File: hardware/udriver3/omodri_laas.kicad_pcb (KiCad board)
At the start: 2 copper layers, 326 parts, among them J1 Conn_01x12, J10 Conn_02x04_Odd_Even, J11 Conn_01x08, J12 Conn_01x08, J2 Conn_01x05, J3 Conn_01x04, J4 Conn_01x02, J5 Conn_01x03, J6 Conn_01x03, J7 Conn_01x05, J8 Conn_01x05, J9 Conn_01x02, Q1 BSC028N06LS3, Q10 BSC028N06LS3, Q11 BSC028N06LS3, Q12 BSC028N06LS3, Q13 BSC028N06LS3, Q14 BSC028N06LS3, Q15 BSC028N06LS3, Q16 CSD88599Q5DC, Q17 CSD88599Q5DC, Q18 CSD88599Q5DC, Q2 BSC028N06LS3, Q3 BSC028N06LS3, Q4 BSC028N06LS3, Q5 BSC028N06LS3, Q6 BSC028N06LS3, Q7 CSD88599Q5DC, Q8 CSD88599Q5DC, Q9 CSD88599Q5DC, SW1 B3U-3100P, U1 DRV8353S, U10 TCAN332G, U11 TPS3703, U12 TPS3703, U13 TPD6E05U06, U14 DSLVDS1048, U15 TPD6E05U06, U16 DSLVDS1047, U17 TPD2E001, U18 TPD2E001, U19 TPD2E001, U2 DRV8353S, U20 TPD2E001, U3 LMZ36002, U4 TMS320F28388D, U5 MPM3804GG, U6 MPM3804GG, U7 REF6230, U8 OPA388, U9 TXB0106, X1 ECS-TXO-2016-33-200-TR

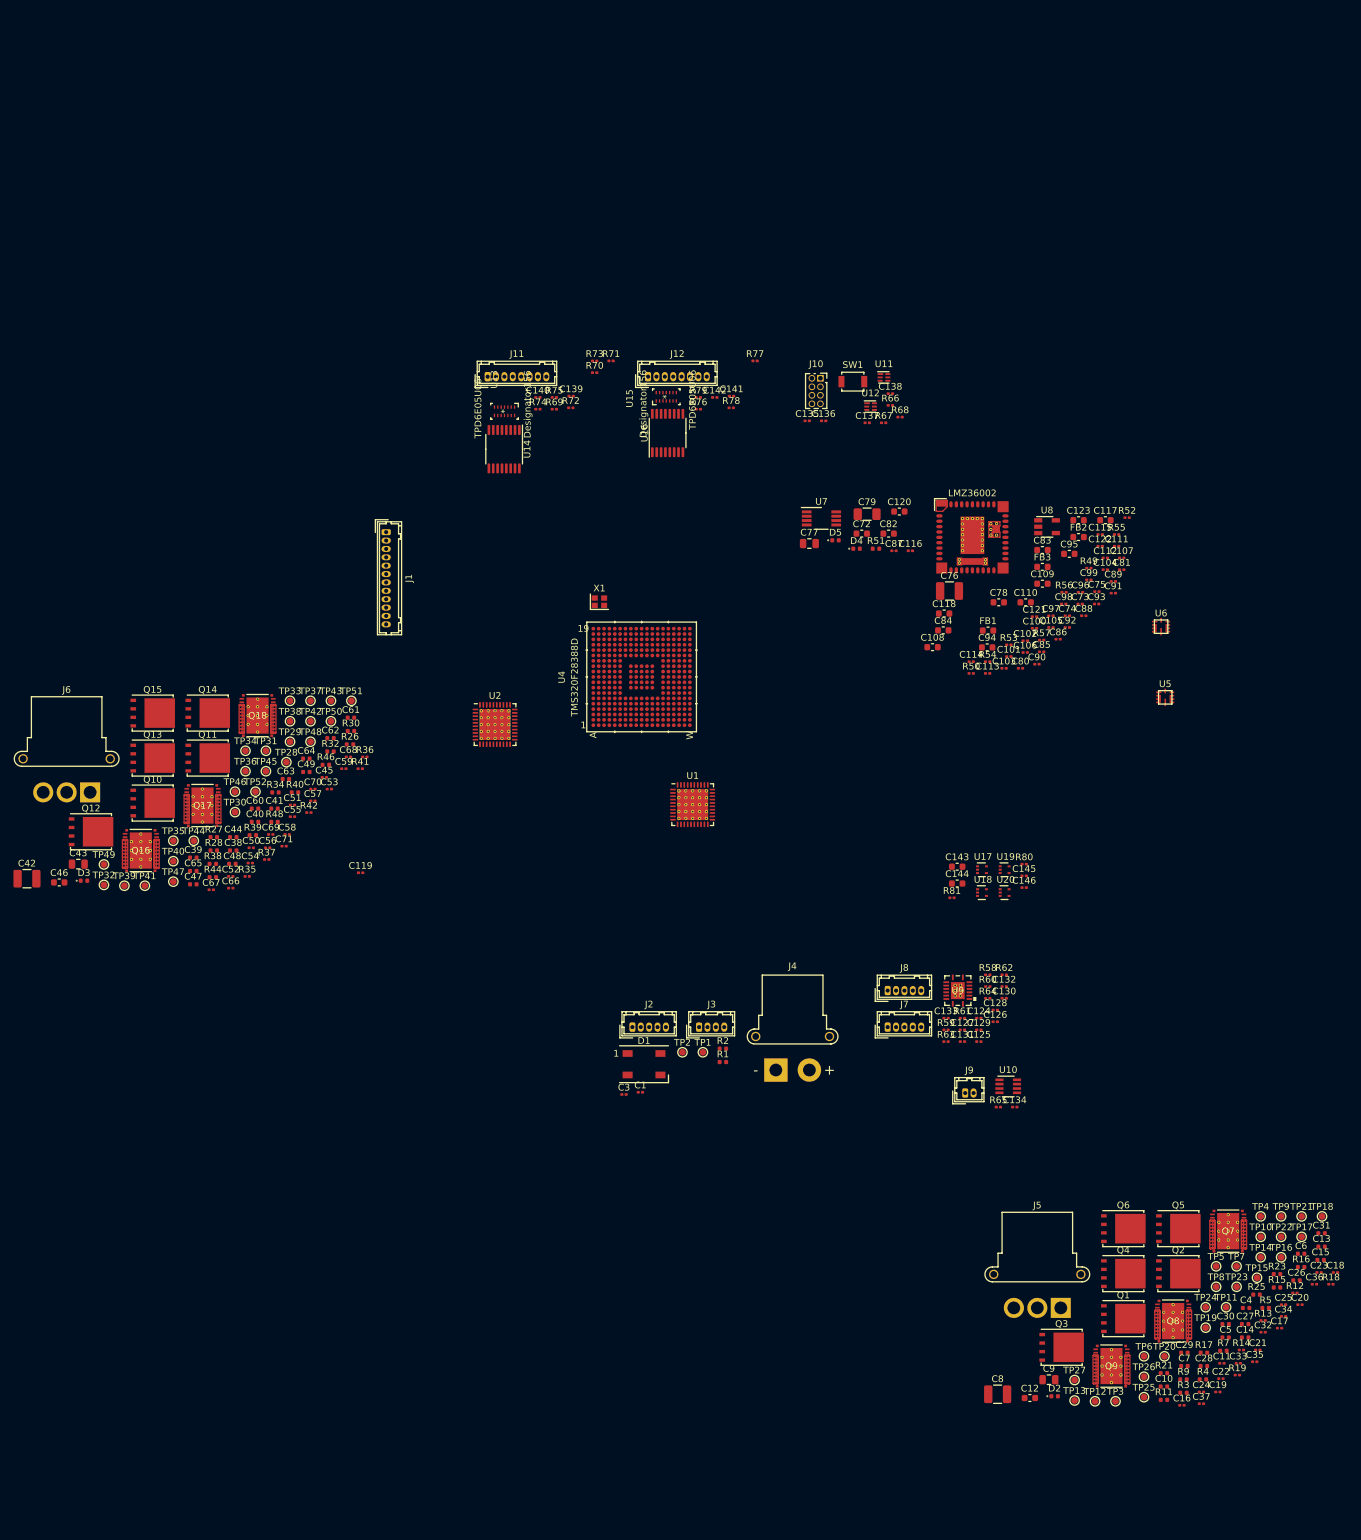
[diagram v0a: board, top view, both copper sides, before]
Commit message: First complete release. No EtherCAT, IO ready to be connected.
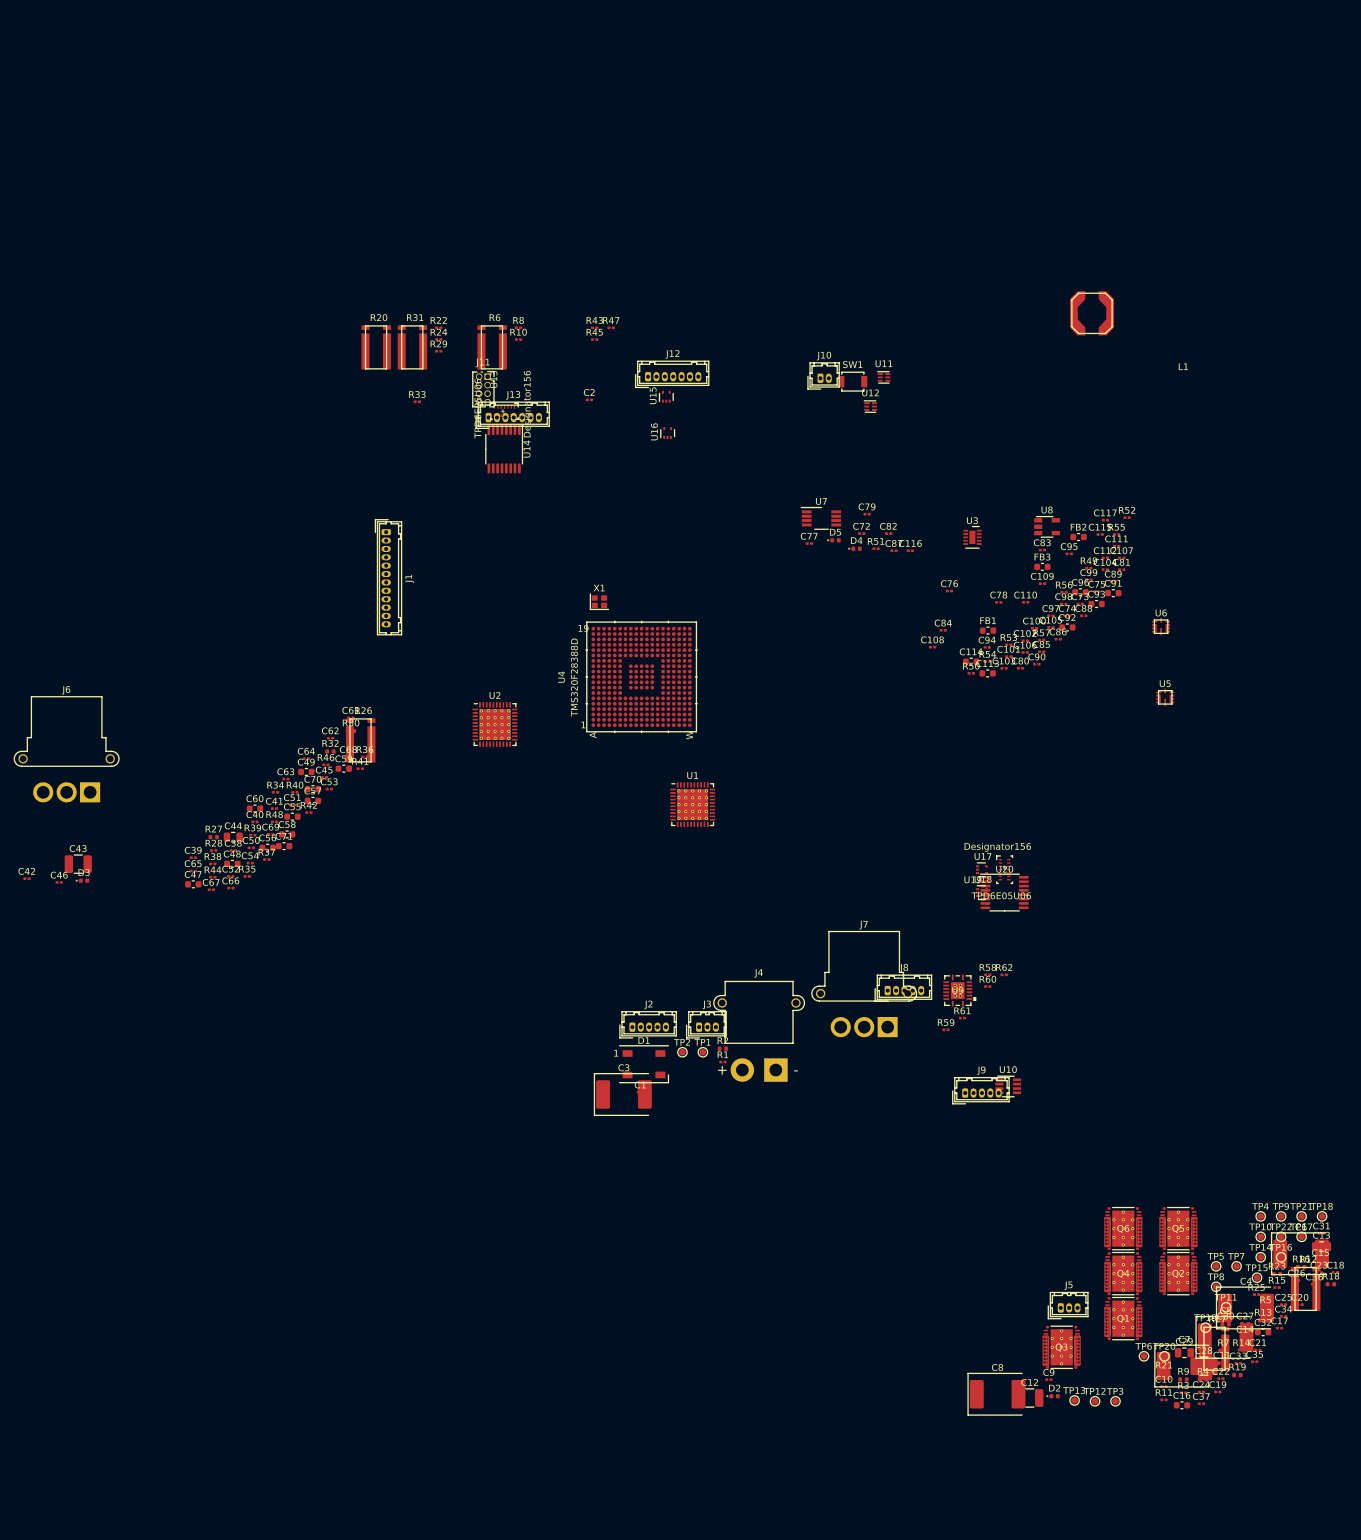
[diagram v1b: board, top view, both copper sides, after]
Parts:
- removed C118, C120, C123, C143, C144: 10uF, Capacitor_SMD:C_0603_1608Metric
- removed C119, C121, C128, C129, C134, C135, C136, C138, C140, C142, C145, C146: 100nF, Capacitor_SMD:C_0201_0603Metric
- removed C122, C127, C133, C139, C141: 1uF, Capacitor_SMD:C_0201_0603Metric
- removed C124, C125, C126, C130, C131, C132: 1nF, Capacitor_SMD:C_0201_0603Metric
- removed C137: 10nF, Capacitor_SMD:C_0201_0603Metric
- removed Q10, Q11, Q12, Q13, Q14, Q15: BSC028N06LS3, Package_TO_SOT_SMD:TDSON-8-1
- removed Q16, Q17, Q18, Q7, Q8, Q9: CSD88599Q5DC, udrive3:VSON_CLIP_22
- removed R63, R64, R68: 1k, Resistor_SMD:R_0201_0603Metric
- removed R65: 120, Resistor_SMD:R_0201_0603Metric
- removed R66, R67, R72, R73, R74, R75, R76, R77, R78, R79: 10k, Resistor_SMD:R_0201_0603Metric
- removed R69, R70, R71: 100, Resistor_SMD:R_0201_0603Metric
- removed R80, R81: 0.1, Resistor_SMD:R_0201_0603Metric
- removed TP23, TP24, TP25, TP26, TP27, TP28, TP29, TP30, TP31, TP32, TP33, TP34, TP35, TP36, TP37, TP38, TP39, TP40, TP41, TP42, TP43, TP44, TP45, TP46, TP47, TP48, TP49, TP50, TP51, TP52: TestPoint, TestPoint:TestPoint_Pad_D1.0mm
- added C2: 10nF, Capacitor_SMD:C_0201_0603Metric, F.Cu at (110.3, -18.5)
- added J13: Conn_01x07, Connector_Hirose:Hirose_DF13-07P-1.25DSA_1x07_P1.25mm_Vertical, F.Cu at (95.3, -15.8)
- added L1: 22uH, udrive3:L_coilcraft_LPS62xx, F.Cu at (185.3, -31.4)
- added R10: 120, Resistor_SMD:R_0201_0603Metric, F.Cu at (99.7, -27.5)
- added R20: 0.005, udrive3:FC4L64, F.Cu at (76.9, -25.7)
- added R22: 120, Resistor_SMD:R_0201_0603Metric, F.Cu at (87.9, -29.2)
- added R24: 120, Resistor_SMD:R_0201_0603Metric, F.Cu at (87.9, -27.5)
- added R29: 10k, Resistor_SMD:R_0201_0603Metric, F.Cu at (87.9, -25.7)
- added R31: 0.005, udrive3:FC4L64, F.Cu at (82.3, -25.7)
- added R33: 10k, Resistor_SMD:R_0201_0603Metric, F.Cu at (84.7, -18.2)
- added R43: 1k, Resistor_SMD:R_0201_0603Metric, F.Cu at (111.1, -29.2)
- added R45: 1k, Resistor_SMD:R_0201_0603Metric, F.Cu at (111.1, -27.5)
- added R47: 1k, Resistor_SMD:R_0201_0603Metric, F.Cu at (113.6, -29.2)
- added R6: 0.005, udrive3:FC4L64, F.Cu at (94.2, -25.7)
- added R8: 120, Resistor_SMD:R_0201_0603Metric, F.Cu at (99.7, -29.2)
- C10, C38: value 1uF -> 10nF; footprint Capacitor_SMD:C_0402_1005Metric -> Capacitor_SMD:C_0201_0603Metric
- C100, C106, C87, C88, C89, C90: value 100nF -> 1uF
- C103, C104, C105, C97, C98, C99: value 100nF -> 1nF
- C108, C109, C117, C72, C82, C83, C84, C94: value 10uF -> 100nF; footprint Capacitor_SMD:C_0603_1608Metric -> Capacitor_SMD:C_0201_0603Metric
- C11: footprint Capacitor_SMD:C_0201_0603Metric -> Capacitor_SMD:C_0402_1005Metric
- C110: value 10uF -> 10nF; footprint Capacitor_SMD:C_0603_1608Metric -> Capacitor_SMD:C_0201_0603Metric
- C113, C114, C91, C92, C93: value 1uF -> 10uF; footprint Capacitor_SMD:C_0201_0603Metric -> Capacitor_SMD:C_0603_1608Metric
- C115, C116, C74, C80: value 1uF -> 100nF
- C12: value 47nF -> 10uF; footprint Capacitor_SMD:C_0603_1608Metric -> Capacitor_SMD:C_1210_3225Metric
- C13, C29: value 1nF -> 100nF; footprint Capacitor_SMD:C_0402_1005Metric -> Capacitor_SMD:C_0805_2012Metric
- C14, C27, C30, C51, C67, C68: value 1nF -> 1uF
- C15, C31: value 1nF -> 1uF; footprint Capacitor_SMD:C_0402_1005Metric -> Capacitor_SMD:C_0201_0603Metric
- C16, C32: value 1nF -> 47nF; footprint Capacitor_SMD:C_0201_0603Metric -> Capacitor_SMD:C_0603_1608Metric
- C18, C34: value 1nF -> 10nF
- C19, C35, C54: value 10nF -> 100nF
- C22: value 100nF -> 10nF
- C23, C25: value 10nF -> 1nF
- C26, C40: value 1nF -> 10nF; footprint Capacitor_SMD:C_0402_1005Metric -> Capacitor_SMD:C_0201_0603Metric
- C28: value 1nF -> 10uF; footprint Capacitor_SMD:C_0402_1005Metric -> Capacitor_SMD:C_1210_3225Metric
- C3: value 10nF -> 100uF; footprint Capacitor_SMD:C_0201_0603Metric -> Capacitor_Tantalum_SMD:CP_EIA-7360-38_Kemet-E
- C39, C41: footprint Capacitor_SMD:C_0402_1005Metric -> Capacitor_SMD:C_0201_0603Metric
- C4: value 1uF -> 100uF; footprint Capacitor_SMD:C_0402_1005Metric -> Capacitor_Tantalum_SMD:CP_EIA-7360-38_Kemet-E
- C42: value 10uF -> 10nF; footprint Capacitor_SMD:C_1210_3225Metric -> Capacitor_SMD:C_0201_0603Metric
- C43: value 100nF -> 10uF; footprint Capacitor_SMD:C_0805_2012Metric -> Capacitor_SMD:C_1210_3225Metric
- C44: value 1uF -> 100nF; footprint Capacitor_SMD:C_0402_1005Metric -> Capacitor_SMD:C_0805_2012Metric
- C45: value 1uF -> 10nF
- C46: value 47nF -> 1uF; footprint Capacitor_SMD:C_0603_1608Metric -> Capacitor_SMD:C_0201_0603Metric
- C47, C48, C49, C60: value 1nF -> 10uF; footprint Capacitor_SMD:C_0402_1005Metric -> Capacitor_SMD:C_0603_1608Metric
- C5, C6, C7: value 1nF -> 100uF; footprint Capacitor_SMD:C_0402_1005Metric -> Capacitor_Tantalum_SMD:CP_EIA-7360-38_Kemet-E
- C50, C52, C66: value 1nF -> 100nF
- C53, C69: value 10nF -> 1uF
- C55, C57, C58, C59, C70, C71: value 10nF -> 10uF; footprint Capacitor_SMD:C_0201_0603Metric -> Capacitor_SMD:C_0603_1608Metric
- C56, C96: value 100nF -> 10uF; footprint Capacitor_SMD:C_0201_0603Metric -> Capacitor_SMD:C_0603_1608Metric
- C61, C62, C63, C64, C65: value 1nF -> 100nF; footprint Capacitor_SMD:C_0402_1005Metric -> Capacitor_SMD:C_0201_0603Metric
- C76: value 10uF -> 100nF; footprint Capacitor_SMD:C_1210_3225Metric -> Capacitor_SMD:C_0201_0603Metric
- C77: footprint Capacitor_SMD:C_0805_2012Metric -> Capacitor_SMD:C_0201_0603Metric
- C78: value 47nF -> 100nF; footprint Capacitor_SMD:C_0603_1608Metric -> Capacitor_SMD:C_0201_0603Metric
- C79: value 100uF -> 100nF; footprint Capacitor_SMD:C_1206_3216Metric -> Capacitor_SMD:C_0201_0603Metric
- C8: value 10uF -> 100uF; footprint Capacitor_SMD:C_1210_3225Metric -> Capacitor_Tantalum_SMD:CP_EIA-7360-38_Kemet-E
- C9: value 100nF -> 10nF; footprint Capacitor_SMD:C_0805_2012Metric -> Capacitor_SMD:C_0201_0603Metric
- C95: value 10uF -> 1uF; footprint Capacitor_SMD:C_0603_1608Metric -> Capacitor_SMD:C_0201_0603Metric
- J10: value Conn_02x04_Odd_Even -> Conn_01x02; footprint Connector_PinSocket_1.27mm:PinSocket_2x04_P1.27mm_Vertical -> Connector_Hirose:Hirose_DF13-02P-1.25DSA_1x02_P1.25mm_Vertical
- J11: value Conn_01x08 -> Conn_02x04_Odd_Even; footprint Connector_Hirose:Hirose_DF13-08P-1.25DSA_1x08_P1.25mm_Vertical -> Connector_PinSocket_1.27mm:PinSocket_2x04_P1.27mm_Vertical
- J12: value Conn_01x08 -> Conn_01x07; footprint Connector_Hirose:Hirose_DF13-08P-1.25DSA_1x08_P1.25mm_Vertical -> Connector_Hirose:Hirose_DF13-07P-1.25DSA_1x07_P1.25mm_Vertical
- J3: value Conn_01x04 -> Conn_01x03; footprint Connector_Hirose:Hirose_DF13-04P-1.25DSA_1x04_P1.25mm_Vertical -> Connector_Hirose:Hirose_DF13-03P-1.25DSA_1x03_P1.25mm_Vertical
- J4: footprint Connector_AMASS:AMASS_XT30PW-F_1x02_P2.50mm_Horizontal -> Connector_AMASS:AMASS_XT30PW-M_1x02_P2.50mm_Horizontal
- J5: footprint Connector_AMASS:AMASS_MR30PW-FB_1x03_P3.50mm_Horizontal -> Connector_Hirose:Hirose_DF13-03P-1.25DSA_1x03_P1.25mm_Vertical
- J7: value Conn_01x05 -> Conn_01x03; footprint Connector_Hirose:Hirose_DF13-05P-1.25DSA_1x05_P1.25mm_Vertical -> Connector_AMASS:AMASS_MR30PW-FB_1x03_P3.50mm_Horizontal
- J9: value Conn_01x02 -> Conn_01x05; footprint Connector_Hirose:Hirose_DF13-02P-1.25DSA_1x02_P1.25mm_Vertical -> Connector_Hirose:Hirose_DF13-05P-1.25DSA_1x05_P1.25mm_Vertical
- Q1, Q2, Q3, Q4, Q5, Q6: value BSC028N06LS3 -> CSD88599Q5DC; footprint Package_TO_SOT_SMD:TDSON-8-1 -> udrive3:VSON_CLIP_22
- R1, R3: value 100k -> 120; footprint Resistor_SMD:R_0402_1005Metric -> Resistor_SMD:R_0201_0603Metric
- R11, R25, R48: value 5.1k -> 120; footprint Resistor_SMD:R_0402_1005Metric -> Resistor_SMD:R_0201_0603Metric
- R12: value 100 -> 0.005; footprint Resistor_SMD:R_0201_0603Metric -> udrive3:FC4L64
- R13: value 100 -> 5.1k; footprint Resistor_SMD:R_0201_0603Metric -> Resistor_SMD:R_0402_1005Metric
- R14, R37: value 100 -> 220
- R15: value 100k -> 10k; footprint Resistor_SMD:R_0402_1005Metric -> Resistor_SMD:R_0201_0603Metric
- R17, R26: value 100k -> 0.005; footprint Resistor_SMD:R_0402_1005Metric -> udrive3:FC4L64
- R18: value 220 -> 5.1k; footprint Resistor_SMD:R_0201_0603Metric -> Resistor_SMD:R_0402_1005Metric
- R19: value 10k -> 100k; footprint Resistor_SMD:R_0201_0603Metric -> Resistor_SMD:R_0402_1005Metric
- R2, R23, R30, R9: value 5.1k -> 100k
- R27, R4: value 100k -> 5.1k
- R28: value 100k -> 220; footprint Resistor_SMD:R_0402_1005Metric -> Resistor_SMD:R_0201_0603Metric
- R34: value 5.1k -> 470; footprint Resistor_SMD:R_0402_1005Metric -> Resistor_SMD:R_0201_0603Metric
- R35: value 100 -> 100k
- R36: value 100 -> 22.1k
- R38, R39: footprint Resistor_SMD:R_0402_1005Metric -> Resistor_SMD:R_0201_0603Metric
- R40: value 100k -> 56; footprint Resistor_SMD:R_0402_1005Metric -> Resistor_SMD:R_0201_0603Metric
- R41: value 220 -> 1k
- R42: value 10k -> 1k
- R44, R46, R51: value 5.1k -> 1k; footprint Resistor_SMD:R_0402_1005Metric -> Resistor_SMD:R_0201_0603Metric
- R49: value 470 -> 10k
- R50: value 150k -> 10k
- R52: value 100k -> 100
- R53: value 22.1k -> 100
- R54: value 220 -> 100
- R55: value 56 -> 10k
- R56, R57: value 100k -> 10k
- R58, R59: value 1k -> 0.1
- R60, R61, R62: value 1k -> 10k
- U15: value TPD6E05U06 -> TPD2E001; footprint udrive3:USON_14 -> Package_SO:Texas_R-PDSO-N5
- U16: value DSLVDS1047 -> TPD2E001; footprint Package_SO:TSSOP-16_4.4x5mm_P0.65mm -> Package_SO:Texas_R-PDSO-N5
- U19: value TPD2E001 -> TPD6E05U06; footprint Package_SO:Texas_R-PDSO-N5 -> udrive3:USON_14
- U20: value TPD2E001 -> DSLVDS1047; footprint Package_SO:Texas_R-PDSO-N5 -> Package_SO:TSSOP-16_4.4x5mm_P0.65mm
- U3: value LMZ36002 -> MAX17502FxTB; footprint udrive3:B3QFN_43 -> Package_DFN_QFN:TDFN-10-1EP_2x3mm_P0.5mm_EP0.9x2mm
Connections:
- C10 pad 1: GND -> /F2838x GPIOs/ANALOG_IN1
- C10 pad 2: /DRV driver for motor2/VGLS -> GND
- C100 pad 1: VDD_3V3 -> 5V0
- C102 pad 1: VDD_3V3 -> 5V0
- C103 pad 1: VDD_3V3 -> /Quadrature Encoders for motor 1 & 2/ENC2_A
- C104 pad 1: VDD_3V3 -> /Quadrature Encoders for motor 1 & 2/ENC2_B
- C105 pad 1: VDD_3V3 -> /Quadrature Encoders for motor 1 & 2/ENC2_I
- C106 pad 1: VDD_3V3 -> 5V0
- C108 pad 1: 5V0 -> VDD_3V3
- C109 pad 1: /Power distribution/1V2 -> VDD_3V3
- C11 pad 1: /DRV driver for motor2/DVDD -> VPOWER
- C11 pad 2: GND -> Net-(C11-Pad2)
- C110 pad 1: /Power distribution/1V2 -> /JTAG Bus + Oscillator + Reset/~XRSn~
- C113 pad 1: VDD_3V3 -> Net-(C113-Pad1)
- C114 pad 1: VDD_3V3 -> Net-(C114-Pad1)
- C115 pad 1: VDD_3V3 -> REF_3V0_BUF
- C116 pad 1: VDD_3V3 -> REF_3V0_BUF
- C12 pad 1: Net-(C12-Pad1) -> VPOWER
- C12 pad 2: Net-(C12-Pad2) -> GND
- C13 pad 1: /DRV driver for motor2/GLA -> VPOWER
- C13 pad 2: Net-(C13-Pad2) -> GND
- C14 pad 1: /DRV driver for motor2/GLB -> GND
- C14 pad 2: Net-(C14-Pad2) -> /DRV driver for motor2/VGLS
- C15 pad 1: /DRV driver for motor2/GLC -> /DRV driver for motor2/DVDD
- C15 pad 2: Net-(C15-Pad2) -> GND
- C16 pad 1: /DRV driver for motor2/SPA -> Net-(C16-Pad1)
- C16 pad 2: /DRV driver for motor2/SNA -> Net-(C16-Pad2)
- C17 pad 1: /DRV driver for motor2/SPB -> /DRV driver for motor2/SPA
- C17 pad 2: /DRV driver for motor2/SNB -> /DRV driver for motor2/SNA
- C18 pad 1: /DRV driver for motor2/SPC -> /F2838x GPIOs/M2_Va
- C18 pad 2: /DRV driver for motor2/SNC -> GND
- C19 pad 1: /F2838x GPIOs/M2_Va -> REF_3V0_BUF
- C20 pad 1: /F2838x GPIOs/M2_Vb -> /F2838x GPIOs/M2_Ic
- C21 pad 1: /F2838x GPIOs/M2_Vc -> /F2838x GPIOs/M2_Ib
- C22 pad 1: REF_3V0_BUF -> /F2838x GPIOs/M2_Ia
- C23 pad 1: /F2838x GPIOs/M2_Ic -> /DRV driver for motor2/SPB
- C23 pad 2: GND -> /DRV driver for motor2/SNB
- C24 pad 1: /F2838x GPIOs/M2_Ib -> /F2838x GPIOs/M2_Vb
- C25 pad 1: /F2838x GPIOs/M2_Ia -> /DRV driver for motor2/SPC
- C25 pad 2: GND -> /DRV driver for motor2/SNC
- C26 pad 1: /DRV driver for motor2/GHA -> /F2838x GPIOs/M2_Vc
- C26 pad 2: /DRV driver for motor2/MOTOR_CH1 -> GND
- C27 pad 1: /DRV driver for motor2/GHB -> VPOWER
- C27 pad 2: /DRV driver for motor2/MOTOR_CH2 -> Net-(C27-Pad2)
- C28 pad 1: /DRV driver for motor2/GHC -> VPOWER
- C28 pad 2: /DRV driver for motor2/MOTOR_CH3 -> GND
- C29 pad 1: /DRV driver for motor2/GLA -> VPOWER
- C29 pad 2: PGND -> GND
- C3 pad 1: /F2838x GPIOs/M1_Vbus -> VPOWER
- C3 pad 2: GND -> Net-(C3-Pad2)
- C30 pad 1: /DRV driver for motor2/GLB -> GND
- C30 pad 2: PGND -> /DRV driver for motor1/VGLS
- C31 pad 1: /DRV driver for motor2/GLC -> /DRV driver for motor1/DVDD
- C31 pad 2: PGND -> GND
- C32 pad 1: /DRV driver for motor2/SPA -> Net-(C32-Pad1)
- C32 pad 2: /DRV driver for motor2/SNA -> Net-(C32-Pad2)
- C33 pad 1: /DRV driver for motor2/SPB -> /DRV driver for motor1/SPA
- C33 pad 2: /DRV driver for motor2/SNB -> /DRV driver for motor1/SNA
- C34 pad 1: /DRV driver for motor2/SPC -> /F2838x GPIOs/M1_Va
- C34 pad 2: /DRV driver for motor2/SNC -> GND
- C35 pad 1: /F2838x GPIOs/M2_Va -> REF_3V0_BUF
- C36 pad 1: /F2838x GPIOs/M2_Vb -> /F2838x GPIOs/M1_Ic
- C37 pad 1: /F2838x GPIOs/M2_Vc -> /F2838x GPIOs/M1_Ib
- C38 pad 1: VPOWER -> /F2838x GPIOs/M1_Ia
- C38 pad 2: Net-(C38-Pad2) -> GND
- C39 pad 1: /DRV driver for motor1/GHA -> /DRV driver for motor1/SPB
- C39 pad 2: /DRV driver for motor1/MOTOR_CH1 -> /DRV driver for motor1/SNB
- C40 pad 1: /DRV driver for motor1/GHB -> /F2838x GPIOs/M1_Vb
- C40 pad 2: /DRV driver for motor1/MOTOR_CH2 -> GND
- C41 pad 1: /DRV driver for motor1/GHC -> /DRV driver for motor1/SPC
- C41 pad 2: /DRV driver for motor1/MOTOR_CH3 -> /DRV driver for motor1/SNC
- C42 pad 1: VPOWER -> /F2838x GPIOs/M1_Vc
- C44 pad 1: GND -> VPOWER
- C44 pad 2: /DRV driver for motor1/VGLS -> GND
- C45 pad 1: /DRV driver for motor1/DVDD -> Net-(C45-Pad1)
- C46 pad 2: Net-(C46-Pad2) -> GND
- C47 pad 1: /DRV driver for motor1/GLA -> 5V0
- C47 pad 2: Net-(C47-Pad2) -> GND
- C48 pad 1: /DRV driver for motor1/GLB -> 5V0
- C48 pad 2: Net-(C48-Pad2) -> GND
- C49 pad 1: /DRV driver for motor1/GLC -> VDDA_3V3
- C49 pad 2: Net-(C49-Pad2) -> GND
- C5 pad 1: /DRV driver for motor2/GHA -> VPOWER
- C5 pad 2: /DRV driver for motor2/MOTOR_CH1 -> Net-(C5-Pad2)
- C50 pad 1: /DRV driver for motor1/SPA -> VDDA_3V3
- C50 pad 2: /DRV driver for motor1/SNA -> GND
- C51 pad 1: /DRV driver for motor1/SPB -> VDD_3V3
- C51 pad 2: /DRV driver for motor1/SNB -> GND
- C52 pad 1: /DRV driver for motor1/SPC -> VDD_3V3
- C52 pad 2: /DRV driver for motor1/SNC -> GND
- C53 pad 1: /F2838x GPIOs/M1_Va -> VDD_3V3
- C54 pad 1: /F2838x GPIOs/M1_Vb -> VDD_3V3
- C55 pad 1: /F2838x GPIOs/M1_Vc -> 5V0
- C56 pad 1: REF_3V0_BUF -> /Power distribution/3V3
- C57 pad 1: /F2838x GPIOs/M1_Ic -> /Power distribution/3V3
- C58 pad 1: /F2838x GPIOs/M1_Ib -> 5V0
- C59 pad 1: /F2838x GPIOs/M1_Ia -> /Power distribution/1V2
- C6 pad 1: /DRV driver for motor2/GHB -> Net-(C3-Pad2)
- C6 pad 2: /DRV driver for motor2/MOTOR_CH2 -> GND
- C60 pad 1: /DRV driver for motor1/GHA -> /Power distribution/1V2
- C60 pad 2: /DRV driver for motor1/MOTOR_CH1 -> GND
- C61 pad 1: /DRV driver for motor1/GHB -> VDD_1V2
- C61 pad 2: /DRV driver for motor1/MOTOR_CH2 -> GND
- C62 pad 1: /DRV driver for motor1/GHC -> VDD_1V2
- C62 pad 2: /DRV driver for motor1/MOTOR_CH3 -> GND
- C63 pad 1: /DRV driver for motor1/GLA -> VDD_1V2
- C63 pad 2: PGND -> GND
- C64 pad 1: /DRV driver for motor1/GLB -> VDD_1V2
- C64 pad 2: PGND -> GND
- C65 pad 1: /DRV driver for motor1/GLC -> VDD_1V2
- C65 pad 2: PGND -> GND
- C66 pad 1: /DRV driver for motor1/SPA -> VDD_1V2
- C66 pad 2: /DRV driver for motor1/SNA -> GND
- C67 pad 1: /DRV driver for motor1/SPB -> VDD_1V2
- C67 pad 2: /DRV driver for motor1/SNB -> GND
- C68 pad 1: /DRV driver for motor1/SPC -> VDD_1V2
- C68 pad 2: /DRV driver for motor1/SNC -> GND
- C69 pad 1: /F2838x GPIOs/M1_Va -> VDD_1V2
- C7 pad 1: /DRV driver for motor2/GHC -> Net-(C4-Pad2)
- C7 pad 2: /DRV driver for motor2/MOTOR_CH3 -> GND
- C70 pad 1: /F2838x GPIOs/M1_Vb -> VDD_1V2
- C71 pad 1: /F2838x GPIOs/M1_Vc -> VDD_1V2
- C72 pad 1: VDDA_3V3 -> VDD_3V3
- C73 pad 1: VDDA_3V3 -> VDD_3V3
- C76 pad 1: VPOWER -> VDD_3V3
- C77 pad 1: VPOWER -> VDD_3V3
- C78 pad 1: Net-(C78-Pad1) -> VDD_3V3
- C79 pad 1: 5V0 -> VDD_3V3
- C8 pad 1: VPOWER -> Net-(C5-Pad2)
- C82 pad 1: 5V0 -> VDD_3V3
- C83 pad 1: /Power distribution/3V3 -> VDD_3V3
- C84 pad 1: /Power distribution/3V3 -> VDDA_3V3
- C85 pad 1: VDD_1V2 -> VDD_3V3
- C86 pad 1: VDD_1V2 -> VDD_3V3
- C87 pad 1: VDD_1V2 -> VDD_3V3
- C88 pad 1: VDD_1V2 -> VDD_3V3
- C89 pad 1: VDD_1V2 -> VDD_3V3
- C9 pad 1: VPOWER -> /F2838x GPIOs/M1_Vbus
- C90 pad 1: VDD_1V2 -> VDD_3V3
- C91 pad 1: VDD_1V2 -> VDD_3V3
- C92 pad 1: VDD_1V2 -> VDD_3V3
- C93 pad 1: VDD_1V2 -> VDDA_3V3
- C94 pad 1: VDD_1V2 -> VDDA_3V3
- C95 pad 1: VDD_1V2 -> Net-(C95-Pad1)
- C96 pad 1: VDD_3V3 -> /Power distribution/REF_3V0
- C97 pad 1: VDD_3V3 -> /Quadrature Encoders for motor 1 & 2/ENC1_A
- C98 pad 1: VDD_3V3 -> /Quadrature Encoders for motor 1 & 2/ENC1_B
- C99 pad 1: VDD_3V3 -> /Quadrature Encoders for motor 1 & 2/ENC1_I
- J1 pad 1: VDDA_3V3 -> GND
- J1 pad 2: GND -> VDD_3V3
- J10 pad 1: /JTAG Bus + Oscillator + Reset/~TRSTn~ -> /CAN Bus link/CAN_H
- J10 pad 2: VDD_3V3 -> /CAN Bus link/CAN_L
- J11 pad 1: /FSI Rx Bus Link/RX_CLK_LVDS_N -> /JTAG Bus + Oscillator + Reset/~TRSTn~
- J11 pad 2: /FSI Rx Bus Link/RX_CLK_LVDS_P -> VDD_3V3
- J11 pad 3: /FSI Rx Bus Link/RX_D0_LVDS_N -> /JTAG Bus + Oscillator + Reset/TCK
- J11 pad 4: /FSI Rx Bus Link/RX_D0_LVDS_P -> GND
- J11 pad 5: /FSI Rx Bus Link/RX_D1_LVDS_N -> /JTAG Bus + Oscillator + Reset/TMS
- J11 pad 6: /FSI Rx Bus Link/RX_D1_LVDS_P -> Net-(J11-Pad6)
- J11 pad 7: VDD_3V3 -> /JTAG Bus + Oscillator + Reset/TDI
- J11 pad 8: GND -> /JTAG Bus + Oscillator + Reset/TDO
- J12 pad 1: /FSI Tx Bus Link/TX_CLK_LVDS_N -> GND
- J12 pad 2: /FSI Tx Bus Link/TX_CLK_LVDS_P -> /FSI Rx Bus Link/RX_CLK_LVDS_N
- J12 pad 3: /FSI Tx Bus Link/TX_D0_LVDS_P -> /FSI Rx Bus Link/RX_CLK_LVDS_P
- J12 pad 4: /FSI Tx Bus Link/TX_D0_LVDS_N -> /FSI Rx Bus Link/RX_D0_LVDS_N
- J12 pad 5: /FSI Tx Bus Link/TX_D1_LVDS_N -> /FSI Rx Bus Link/RX_D0_LVDS_P
- J12 pad 6: /FSI Tx Bus Link/TX_D1_LVDS_P -> /FSI Rx Bus Link/RX_D1_LVDS_N
- J12 pad 7: VDD_3V3 -> /FSI Rx Bus Link/RX_D1_LVDS_P
- J3 pad 1: VDDA_3V3 -> GND
- J3 pad 2: /F2838x GPIOs/ANALOG_IN1 -> Net-(J3-Pad2)
- J3 pad 3: GND -> VDDA_3V3
- J5 pad 1: /DRV driver for motor2/MOTOR_CH1 -> GND
- J5 pad 2: /DRV driver for motor2/MOTOR_CH2 -> Net-(J5-Pad2)
- J5 pad 3: /DRV driver for motor2/MOTOR_CH3 -> VDDA_3V3
- J6 pad 1: /DRV driver for motor1/MOTOR_CH1 -> /DRV driver for motor2/MOTOR_CH1
- J6 pad 2: /DRV driver for motor1/MOTOR_CH2 -> /DRV driver for motor2/MOTOR_CH2
- J6 pad 3: /DRV driver for motor1/MOTOR_CH3 -> /DRV driver for motor2/MOTOR_CH3
- J7 pad 1: /Quadrature Encoders for motor 1 & 2/ENC1_A -> /DRV driver for motor1/MOTOR_CH1
- J7 pad 2: /Quadrature Encoders for motor 1 & 2/ENC1_B -> /DRV driver for motor1/MOTOR_CH2
- J7 pad 3: /Quadrature Encoders for motor 1 & 2/ENC1_I -> /DRV driver for motor1/MOTOR_CH3
- J8 pad 1: /Quadrature Encoders for motor 1 & 2/ENC2_A -> /Quadrature Encoders for motor 1 & 2/ENC1_A
- J8 pad 2: /Quadrature Encoders for motor 1 & 2/ENC2_B -> /Quadrature Encoders for motor 1 & 2/ENC1_B
- J8 pad 3: /Quadrature Encoders for motor 1 & 2/ENC2_I -> /Quadrature Encoders for motor 1 & 2/ENC1_I
- J9 pad 1: /CAN Bus link/CAN_H -> /Quadrature Encoders for motor 1 & 2/ENC2_A
- J9 pad 2: /CAN Bus link/CAN_L -> /Quadrature Encoders for motor 1 & 2/ENC2_B
- Q1 pad 1: /DRV driver for motor2/MOTOR_CH1 -> /DRV driver for motor2/GHA
- Q1 pad 2: /DRV driver for motor2/MOTOR_CH1 -> /DRV driver for motor2/SHA
- Q1 pad 4: /DRV driver for motor2/GHA -> /DRV driver for motor2/MOTOR_CH1
- Q1 pad 5: VPOWER -> /DRV driver for motor2/MOTOR_CH1
- Q2 pad 1: /DRV driver for motor2/MOTOR_CH2 -> /DRV driver for motor2/GHB
- Q2 pad 2: /DRV driver for motor2/MOTOR_CH2 -> /DRV driver for motor2/SHB
- Q2 pad 4: /DRV driver for motor2/GHB -> /DRV driver for motor2/MOTOR_CH2
- Q2 pad 5: VPOWER -> /DRV driver for motor2/MOTOR_CH2
- Q3 pad 1: /DRV driver for motor2/MOTOR_CH3 -> /DRV driver for motor2/GHC
- Q3 pad 2: /DRV driver for motor2/MOTOR_CH3 -> /DRV driver for motor2/SHC
- Q3 pad 4: /DRV driver for motor2/GHC -> /DRV driver for motor2/MOTOR_CH3
- Q3 pad 5: VPOWER -> /DRV driver for motor2/MOTOR_CH3
- Q4 pad 1: Net-(C13-Pad2) -> /DRV driver for motor1/GHA
- Q4 pad 2: Net-(C13-Pad2) -> /DRV driver for motor1/SHA
- Q4 pad 3: Net-(C13-Pad2) -> /DRV driver for motor1/MOTOR_CH1
- Q4 pad 4: /DRV driver for motor2/GLA -> /DRV driver for motor1/MOTOR_CH1
- Q4 pad 5: /DRV driver for motor2/MOTOR_CH1 -> /DRV driver for motor1/MOTOR_CH1
- Q5 pad 1: Net-(C14-Pad2) -> /DRV driver for motor1/GHB
- Q5 pad 2: Net-(C14-Pad2) -> /DRV driver for motor1/SHB
- Q5 pad 3: Net-(C14-Pad2) -> /DRV driver for motor1/MOTOR_CH2
- Q5 pad 4: /DRV driver for motor2/GLB -> /DRV driver for motor1/MOTOR_CH2
- Q5 pad 5: /DRV driver for motor2/MOTOR_CH2 -> /DRV driver for motor1/MOTOR_CH2
- Q6 pad 1: Net-(C15-Pad2) -> /DRV driver for motor1/GHC
- Q6 pad 2: Net-(C15-Pad2) -> /DRV driver for motor1/SHC
- Q6 pad 3: Net-(C15-Pad2) -> /DRV driver for motor1/MOTOR_CH3
- Q6 pad 4: /DRV driver for motor2/GLC -> /DRV driver for motor1/MOTOR_CH3
- Q6 pad 5: /DRV driver for motor2/MOTOR_CH3 -> /DRV driver for motor1/MOTOR_CH3
- R1 pad 1: VPOWER -> /F2838x GPIOs/ANALOG_IN2
- R1 pad 2: /F2838x GPIOs/M1_Vbus -> Net-(J3-Pad2)
- R11 pad 1: /F2838x GPIOs/M2_Vc -> /F2838x GPIOs/M2_Ia
- R11 pad 2: GND -> Net-(R11-Pad2)
- R12 pad 1: /F2838x GPIOs/M2_Ic -> GND
- R12 pad 2: Net-(R12-Pad2) -> /DRV driver for motor2/SNB
- R13 pad 1: /F2838x GPIOs/M2_Ib -> /F2838x GPIOs/M2_Vb
- R13 pad 2: Net-(R13-Pad2) -> GND
- R14 pad 1: /F2838x GPIOs/M2_Ia -> /F2838x GPIOs/~DRV2_GPIO_FAULTn~
- R14 pad 2: Net-(R14-Pad2) -> Net-(D2-Pad1)
- R15 pad 1: /DRV driver for motor2/MOTOR_CH1 -> /F2838x GPIOs/~DRV2_GPIO_FAULTn~
- R15 pad 2: /F2838x GPIOs/M2_Va -> VDD_3V3
- R16 pad 1: /DRV driver for motor2/MOTOR_CH2 -> /DRV driver for motor2/MOTOR_CH3
- R16 pad 2: /F2838x GPIOs/M2_Vb -> /F2838x GPIOs/M2_Vc
- R17 pad 1: /DRV driver for motor2/MOTOR_CH3 -> GND
- R17 pad 2: /F2838x GPIOs/M2_Vc -> /DRV driver for motor2/SNC
- R18 pad 1: /F2838x GPIOs/~DRV2_GPIO_FAULTn~ -> /F2838x GPIOs/M2_Vc
- R18 pad 2: Net-(D2-Pad1) -> GND
- R19 pad 1: /F2838x GPIOs/~DRV2_GPIO_FAULTn~ -> /DRV driver for motor1/MOTOR_CH1
- R19 pad 2: VDD_3V3 -> /F2838x GPIOs/M1_Va
- R2 pad 1: /F2838x GPIOs/M1_Vbus -> VPOWER
- R2 pad 2: GND -> /F2838x GPIOs/M1_Vbus
- R21 pad 1: /F2838x GPIOs/M2_Va -> /F2838x GPIOs/M1_Va
- R23 pad 1: /F2838x GPIOs/M2_Vb -> /DRV driver for motor1/MOTOR_CH2
- R23 pad 2: GND -> /F2838x GPIOs/M1_Vb
- R25 pad 1: /F2838x GPIOs/M2_Vc -> /F2838x GPIOs/M1_Ia
- R25 pad 2: GND -> Net-(R25-Pad2)
- R26 pad 1: /DRV driver for motor1/MOTOR_CH1 -> GND
- R26 pad 2: /F2838x GPIOs/M1_Va -> /DRV driver for motor1/SNB
- R27 pad 1: /DRV driver for motor1/MOTOR_CH2 -> /F2838x GPIOs/M1_Vb
- R27 pad 2: /F2838x GPIOs/M1_Vb -> GND
- R28 pad 1: /DRV driver for motor1/MOTOR_CH3 -> /F2838x GPIOs/~DRV1_GPIO_FAULTn~
- R28 pad 2: /F2838x GPIOs/M1_Vc -> Net-(D3-Pad1)
- R3 pad 1: /DRV driver for motor2/MOTOR_CH1 -> /F2838x GPIOs/ANALOG_IN1
- R3 pad 2: /F2838x GPIOs/M2_Va -> Net-(J5-Pad2)
- R30 pad 1: /F2838x GPIOs/M1_Va -> /DRV driver for motor1/MOTOR_CH3
- R30 pad 2: GND -> /F2838x GPIOs/M1_Vc
- R32 pad 1: /F2838x GPIOs/M1_Vb -> /F2838x GPIOs/M1_Vc
- R34 pad 1: /F2838x GPIOs/M1_Vc -> Net-(D4-Pad1)
- R35 pad 1: /F2838x GPIOs/M1_Ic -> /Power distribution/3V3
- R35 pad 2: Net-(R35-Pad2) -> /Power distribution/FB_3V3
- R36 pad 1: /F2838x GPIOs/M1_Ib -> /Power distribution/FB_3V3
- R36 pad 2: Net-(R36-Pad2) -> GND
- R37 pad 1: /F2838x GPIOs/M1_Ia -> Net-(D5-Pad1)
- R37 pad 2: Net-(R37-Pad2) -> GND
- R38 pad 1: /DRV driver for motor1/MOTOR_CH1 -> /Power distribution/1V2
- R38 pad 2: /F2838x GPIOs/M1_Va -> /Power distribution/FB_1V2
- R39 pad 1: /DRV driver for motor1/MOTOR_CH2 -> /Power distribution/FB_1V2
- R39 pad 2: /F2838x GPIOs/M1_Vb -> GND
- R4 pad 1: /DRV driver for motor2/MOTOR_CH2 -> /F2838x GPIOs/M1_Vbus
- R4 pad 2: /F2838x GPIOs/M2_Vb -> GND
- R40 pad 1: /DRV driver for motor1/MOTOR_CH3 -> VDD_1V2
- R40 pad 2: /F2838x GPIOs/M1_Vc -> GND
- R41 pad 1: /F2838x GPIOs/~DRV1_GPIO_FAULTn~ -> 5V0
- R41 pad 2: Net-(D3-Pad1) -> /Quadrature Encoders for motor 1 & 2/ENC1_A
- R42 pad 1: /F2838x GPIOs/~DRV1_GPIO_FAULTn~ -> 5V0
- R42 pad 2: VDD_3V3 -> /Quadrature Encoders for motor 1 & 2/ENC1_B
- R44 pad 1: /F2838x GPIOs/M1_Va -> 5V0
- R44 pad 2: GND -> /Quadrature Encoders for motor 1 & 2/ENC2_A
- R46 pad 1: /F2838x GPIOs/M1_Vb -> 5V0
- R46 pad 2: GND -> /Quadrature Encoders for motor 1 & 2/ENC2_I
- R48 pad 1: /F2838x GPIOs/M1_Vc -> /CAN Bus link/CAN_H
- R48 pad 2: GND -> /CAN Bus link/CAN_L
- R49 pad 1: Net-(D4-Pad1) -> Net-(R49-Pad1)
- R5 pad 1: /DRV driver for motor2/MOTOR_CH3 -> /DRV driver for motor2/MOTOR_CH1
- R5 pad 2: /F2838x GPIOs/M2_Vc -> /F2838x GPIOs/M2_Va
- R50 pad 1: Net-(R50-Pad1) -> VDD_3V3
- R50 pad 2: GND -> /JTAG Bus + Oscillator + Reset/~XRSn~
- R51 pad 1: Net-(R51-Pad1) -> /JTAG Bus + Oscillator + Reset/~TRSTn~
- R52 pad 1: /Power distribution/3V3 -> /FSI Rx Bus Link/RX_CLK_LVDS_P
- R52 pad 2: /Power distribution/FB_3V3 -> /FSI Rx Bus Link/RX_CLK_LVDS_N
- R53 pad 1: /Power distribution/FB_3V3 -> /FSI Rx Bus Link/RX_D0_LVDS_P
- R53 pad 2: GND -> /FSI Rx Bus Link/RX_D0_LVDS_N
- R54 pad 1: Net-(D5-Pad1) -> /FSI Rx Bus Link/RX_D1_LVDS_P
- R54 pad 2: GND -> /FSI Rx Bus Link/RX_D1_LVDS_N
- R55 pad 1: VDD_1V2 -> GND
- R55 pad 2: GND -> /F2838x GPIOs/FSI_RXA_CLK
- R56 pad 1: /Power distribution/1V2 -> GND
- R56 pad 2: /Power distribution/FB_1V2 -> /F2838x GPIOs/FSI_RXA_D0
- R57 pad 1: /Power distribution/FB_1V2 -> GND
- R57 pad 2: GND -> /F2838x GPIOs/FSI_RXA_D1
- R58 pad 1: 5V0 -> REF_3V0_BUF
- R58 pad 2: /Quadrature Encoders for motor 1 & 2/ENC1_A -> Net-(C113-Pad1)
- R59 pad 1: 5V0 -> REF_3V0_BUF
- R59 pad 2: /Quadrature Encoders for motor 1 & 2/ENC1_B -> Net-(C114-Pad1)
- R60 pad 1: 5V0 -> GND
- R60 pad 2: /Quadrature Encoders for motor 1 & 2/ENC1_I -> /F2838x GPIOs/FSI_TXA_D0
- R61 pad 1: 5V0 -> GND
- R61 pad 2: /Quadrature Encoders for motor 1 & 2/ENC2_A -> /F2838x GPIOs/FSI_TXA_D1
- R62 pad 1: 5V0 -> GND
- R62 pad 2: /Quadrature Encoders for motor 1 & 2/ENC2_B -> /F2838x GPIOs/FSI_TXA_CLK
- R9 pad 1: /F2838x GPIOs/M2_Vb -> /DRV driver for motor2/MOTOR_CH2
- R9 pad 2: GND -> /F2838x GPIOs/M2_Vb
- TP10 pad 1: /DRV driver for motor2/GLA -> /DRV driver for motor2/GHC
- TP11 pad 1: /DRV driver for motor2/GLB -> /DRV driver for motor2/GLC
- TP12 pad 1: /DRV driver for motor2/GLC -> /F2838x GPIOs/M2_Vc
- TP13 pad 1: /F2838x GPIOs/M2_Va -> /DRV driver for motor1/GHA
- TP14 pad 1: /F2838x GPIOs/M2_Vb -> Net-(C27-Pad2)
- TP15 pad 1: /F2838x GPIOs/M2_Vc -> /DRV driver for motor1/GLA
- TP16 pad 1: /DRV driver for motor2/GHA -> /F2838x GPIOs/M1_Va
- TP17 pad 1: /DRV driver for motor2/GHB -> /DRV driver for motor1/GHB
- TP18 pad 1: /DRV driver for motor2/GHC -> /DRV driver for motor1/GLB
- TP19 pad 1: /DRV driver for motor2/MOTOR_CH1 -> /F2838x GPIOs/M1_Vb
- TP20 pad 1: /DRV driver for motor2/MOTOR_CH2 -> /DRV driver for motor1/GHC
- TP21 pad 1: /DRV driver for motor2/MOTOR_CH3 -> /DRV driver for motor1/GLC
- TP22 pad 1: /DRV driver for motor2/GLA -> /F2838x GPIOs/M1_Vc
- TP3 pad 1: Net-(C4-Pad2) -> /DRV driver for motor2/GHA
- TP4 pad 1: /DRV driver for motor2/GHA -> Net-(C11-Pad2)
- TP5 pad 1: /DRV driver for motor2/GHB -> /DRV driver for motor2/GLA
- TP6 pad 1: /DRV driver for motor2/GHC -> /F2838x GPIOs/M2_Va
- TP7 pad 1: /DRV driver for motor2/MOTOR_CH1 -> /DRV driver for motor2/GHB
- TP8 pad 1: /DRV driver for motor2/MOTOR_CH2 -> /DRV driver for motor2/GLB
- TP9 pad 1: /DRV driver for motor2/MOTOR_CH3 -> /F2838x GPIOs/M2_Vb
- U1 pad 1: Net-(C12-Pad2) -> Net-(C16-Pad2)
- U1 pad 14: /DRV driver for motor2/MOTOR_CH2 -> /DRV driver for motor2/SHB
- U1 pad 17: /DRV driver for motor2/MOTOR_CH3 -> /DRV driver for motor2/SHC
- U1 pad 2: Net-(C12-Pad1) -> Net-(C16-Pad1)
- U1 pad 21: Net-(R12-Pad2) -> Net-(R8-Pad2)
- U1 pad 22: Net-(R13-Pad2) -> Net-(R10-Pad2)
- U1 pad 23: Net-(R14-Pad2) -> Net-(R11-Pad2)
- U1 pad 5: Net-(C4-Pad2) -> Net-(C11-Pad2)
- U1 pad 7: /DRV driver for motor2/MOTOR_CH1 -> /DRV driver for motor2/SHA
- U14 pad 16: /F2838x GPIOs/FSI_RX_EN -> VDD_3V3
- U15 pad 1: /FSI Tx Bus Link/TX_CLK_LVDS_N -> VDDA_3V3
- U15 pad 2: /FSI Tx Bus Link/TX_CLK_LVDS_P -> /F2838x GPIOs/ANALOG_IN2
- U15 pad 3: /FSI Tx Bus Link/TX_D0_LVDS_P -> /F2838x GPIOs/ANALOG_IN1
- U15 pad 4: /FSI Tx Bus Link/TX_D0_LVDS_N -> GND
- U15 pad 5: GND -> /F2838x GPIOs/ANALOG_IN2
- U16 pad 1: /F2838x GPIOs/FSI_TX_EN -> VDDA_3V3
- U16 pad 2: /F2838x GPIOs/FSI_TXA_D0 -> /F2838x GPIOs/M2_Vb
- U16 pad 3: /F2838x GPIOs/FSI_TXA_D1 -> /F2838x GPIOs/M1_Vb
- U16 pad 4: VDD_3V3 -> GND
- U16 pad 5: GND -> /F2838x GPIOs/M2_Vb
- U17 pad 2: /F2838x GPIOs/ANALOG_IN2 -> /F2838x GPIOs/M2_Va
- U17 pad 3: /F2838x GPIOs/ANALOG_IN1 -> /F2838x GPIOs/M1_Va
- U17 pad 5: /F2838x GPIOs/ANALOG_IN2 -> /F2838x GPIOs/M2_Va
- U18 pad 2: /F2838x GPIOs/M2_Vb -> /F2838x GPIOs/M2_Vc
- U18 pad 3: /F2838x GPIOs/M1_Vb -> /F2838x GPIOs/M1_Vc
- U18 pad 5: /F2838x GPIOs/M2_Vb -> /F2838x GPIOs/M2_Vc
- U19 pad 1: VDDA_3V3 -> /FSI Tx Bus Link/TX_CLK_LVDS_N
- U19 pad 2: /F2838x GPIOs/M2_Va -> /FSI Tx Bus Link/TX_CLK_LVDS_P
- U19 pad 3: /F2838x GPIOs/M1_Va -> /FSI Tx Bus Link/TX_D0_LVDS_P
- U19 pad 4: GND -> /FSI Tx Bus Link/TX_D0_LVDS_N
- U19 pad 5: /F2838x GPIOs/M2_Va -> GND
- U2 pad 1: Net-(C46-Pad2) -> Net-(C32-Pad2)
- U2 pad 14: /DRV driver for motor1/MOTOR_CH2 -> /DRV driver for motor1/SHB
- U2 pad 17: /DRV driver for motor1/MOTOR_CH3 -> /DRV driver for motor1/SHC
- U2 pad 2: Net-(C46-Pad1) -> Net-(C32-Pad1)
- U2 pad 21: Net-(R35-Pad2) -> Net-(R22-Pad2)
- U2 pad 22: Net-(R36-Pad2) -> Net-(R24-Pad2)
- U2 pad 23: Net-(R37-Pad2) -> Net-(R25-Pad2)
- U2 pad 5: Net-(C38-Pad2) -> Net-(C27-Pad2)
- U2 pad 7: /DRV driver for motor1/MOTOR_CH1 -> /DRV driver for motor1/SHA
- U20 pad 1: VDDA_3V3 -> VDD_3V3
- U20 pad 2: /F2838x GPIOs/M2_Vc -> /F2838x GPIOs/FSI_TXA_D0
- U20 pad 3: /F2838x GPIOs/M1_Vc -> /F2838x GPIOs/FSI_TXA_D1
- U20 pad 4: GND -> VDD_3V3
- U20 pad 5: /F2838x GPIOs/M2_Vc -> GND
- U3 pad 2: GND -> VPOWER
- U3 pad 3: GND -> VPOWER
- U3 pad 4: GND -> Net-(C46-Pad1)
- U3 pad 5: GND -> 5V0
- U3 pad 6: Net-(U3-Pad6) -> Net-(C45-Pad1)
- U3 pad 7: 5V0 -> Net-(U3-Pad7)
- U3 pad 8: GND -> /Power distribution/PG_5V0
- U3 pad 9: Net-(R50-Pad1) -> GND
- U4 pad P19: /F2838x GPIOs/FSI_RX_EN -> Net-(U4-PadP19)
- U4 pad T19: /F2838x GPIOs/FSI_TX_EN -> Net-(U4-PadT19)
- U4 pad U19: Net-(R66-Pad1) -> Net-(R49-Pad1)
- U7 pad 4: Net-(C122-Pad1) -> Net-(C95-Pad1)
